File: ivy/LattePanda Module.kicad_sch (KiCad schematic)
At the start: 1 part

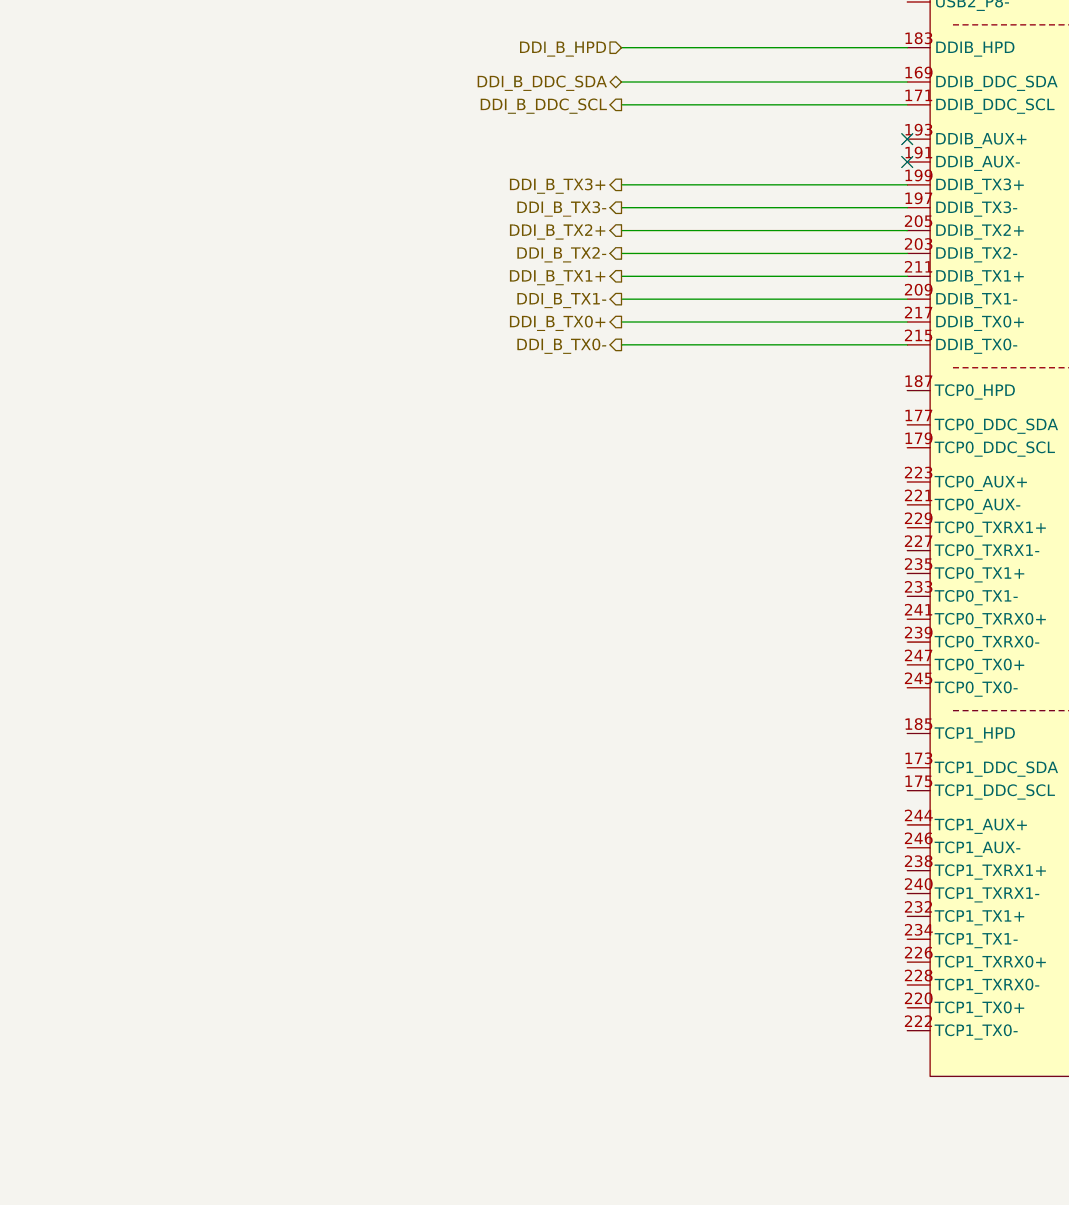
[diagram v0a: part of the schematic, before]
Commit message: create USB sheet
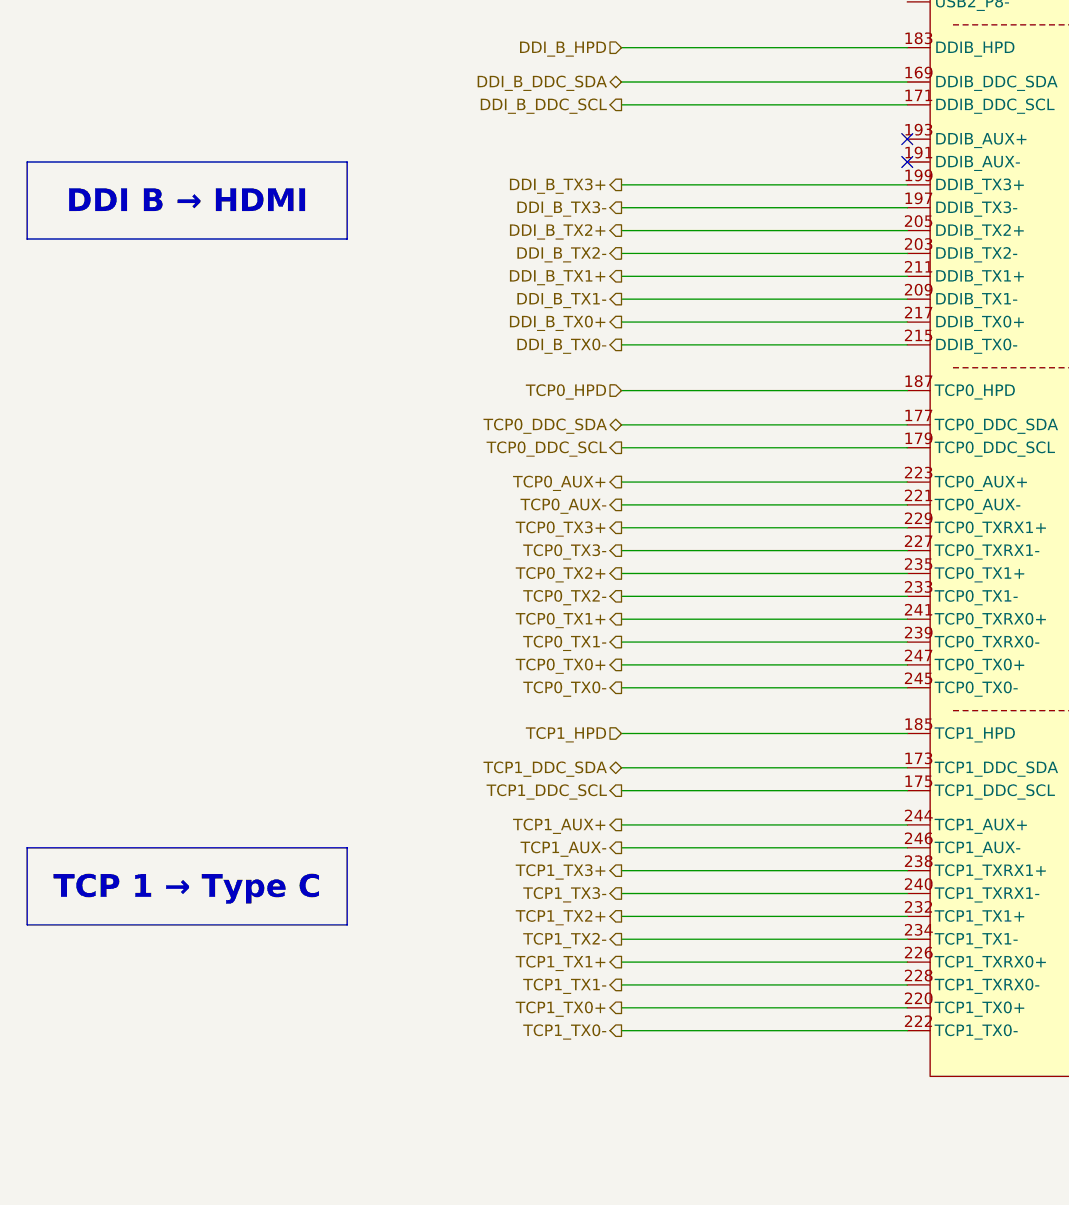
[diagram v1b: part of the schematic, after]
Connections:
- net TCP1_DDC_SDA: now reaches A1.173 (TCP1_DDC_SDA)
- net TCP1_DDC_SCL: now reaches A1.175 (TCP1_DDC_SCL)
- net TCP0_DDC_SDA: now reaches A1.177 (TCP0_DDC_SDA)
- net TCP0_DDC_SCL: now reaches A1.179 (TCP0_DDC_SCL)
- net TCP1_HPD: now reaches A1.185 (TCP1_HPD)
- net TCP0_HPD: now reaches A1.187 (TCP0_HPD)
- net TCP1_TX0+: now reaches A1.220 (TCP1_TX0+)
- net TCP0_AUX-: now reaches A1.221 (TCP0_AUX-)
- net TCP1_TX0-: now reaches A1.222 (TCP1_TX0-)
- net TCP0_AUX+: now reaches A1.223 (TCP0_AUX+)
- net TCP1_TX1+: now reaches A1.226 (TCP1_TXRX0+)
- net TCP0_TX3-: now reaches A1.227 (TCP0_TXRX1-)
- net TCP1_TX1-: now reaches A1.228 (TCP1_TXRX0-)
- net TCP0_TX3+: now reaches A1.229 (TCP0_TXRX1+)
- net TCP1_TX2+: now reaches A1.232 (TCP1_TX1+)
- net TCP0_TX2-: now reaches A1.233 (TCP0_TX1-)
- net TCP1_TX2-: now reaches A1.234 (TCP1_TX1-)
- net TCP0_TX2+: now reaches A1.235 (TCP0_TX1+)
- net TCP1_TX3+: now reaches A1.238 (TCP1_TXRX1+)
- net TCP0_TX1-: now reaches A1.239 (TCP0_TXRX0-)
- net TCP1_TX3-: now reaches A1.240 (TCP1_TXRX1-)
- net TCP0_TX1+: now reaches A1.241 (TCP0_TXRX0+)
- net TCP1_AUX+: now reaches A1.244 (TCP1_AUX+)
- net TCP0_TX0-: now reaches A1.245 (TCP0_TX0-)
- net TCP1_AUX-: now reaches A1.246 (TCP1_AUX-)
- net TCP0_TX0+: now reaches A1.247 (TCP0_TX0+)
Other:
- title: (none) -> LattePanda Mu SODIMM Connector
